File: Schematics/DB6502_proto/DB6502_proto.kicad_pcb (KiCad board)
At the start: 2 copper layers, 143.5 x 138.4 mm, 96 parts, among them J1 Power plug, J10 System Bus, J11 LCD Port, J12 VIA Ports, J13 UART GPIO, J2 Controls, J3 AVR ISP, J4 Debug USB, J5 JPR, J6 Debug UART, J7 UART A, J8 UART B, J9 I/O Bus, SW1 Reset, U1 71256, U10 FT230XS, U11 74HC595, U12 74HC157, U13 ATmega644PA-PU, U14 74AC74, U15 DS1813, U16 74AC74, U17 74AC08, U18 SC26C92, U19 65C22S, U2 71256, U20 74AC04, U21 74AC574, U3 28C256, U4 65C02S, U5 74AC74, U6 74AC138, U7 22V10C, U8 74AC04, U9 74HC21, X1 8MHz, Y1 20MHz, Y2 3,6864MHz

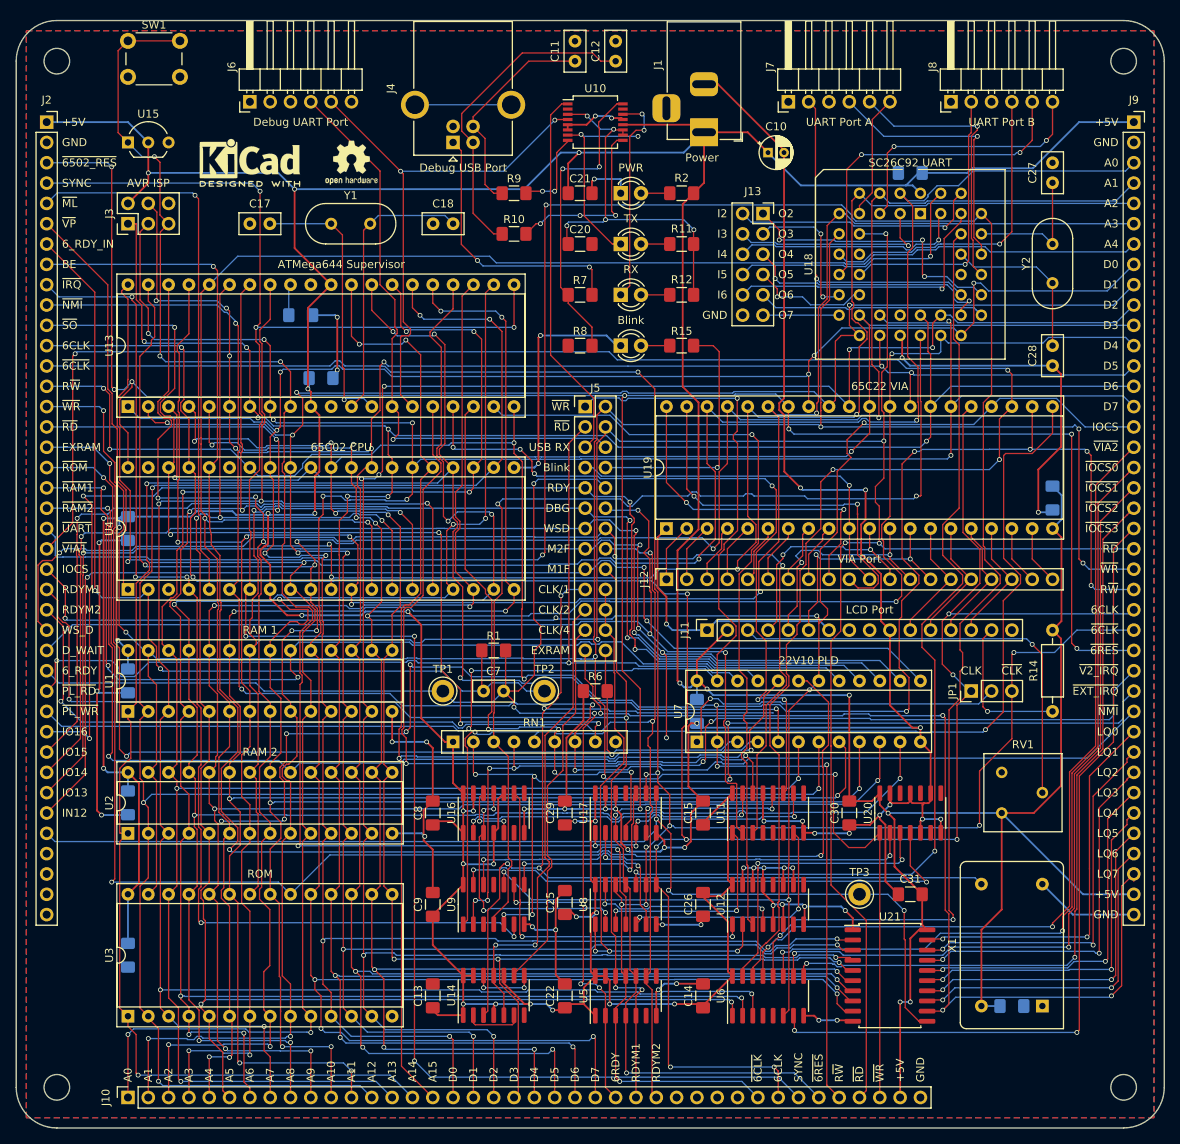
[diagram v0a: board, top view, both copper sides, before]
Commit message: Added bus labels
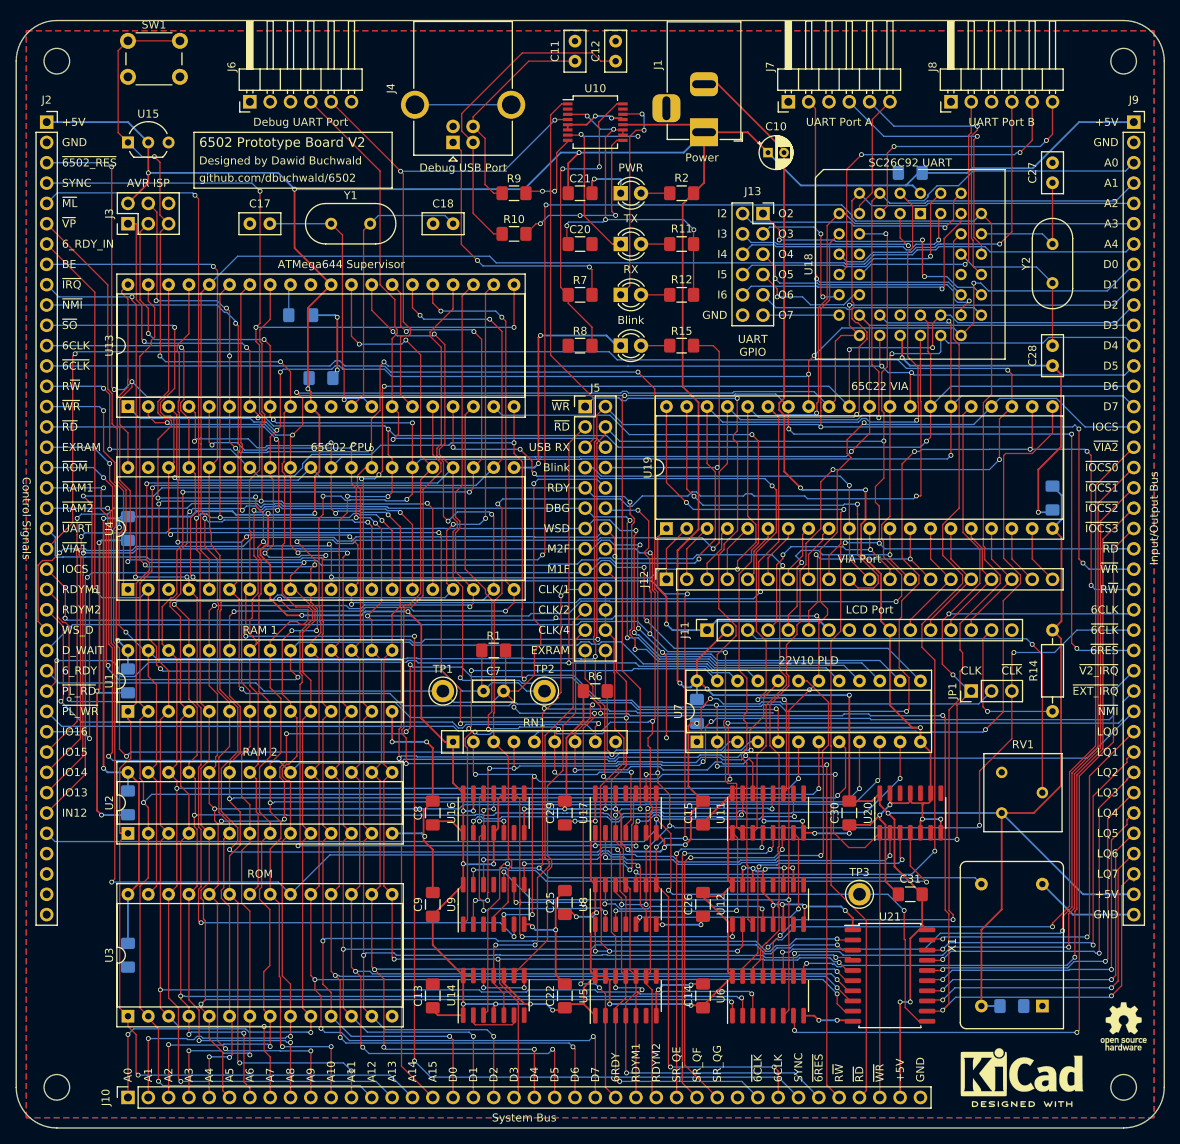
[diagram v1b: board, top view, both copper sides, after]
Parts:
- removed the REF** at (63.5, 53.3)
- removed the REF** at (50.8, 53.3)
- added REF**: OSHW-Logo_5.7x6mm_SilkScreen, Symbol:OSHW-Logo_5.7x6mm_SilkScreen, F.Cu at (160.0, 161.3)
- added REF**: KiCad-Logo2_6mm_SilkScreen, Symbol:KiCad-Logo2_6mm_SilkScreen, F.Cu at (147.3, 167.0)
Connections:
- J10 pad 28: Net-(J10-Pad28) -> SR_QE
- J10 pad 29: Net-(J10-Pad29) -> SR_QF
- J10 pad 30: Net-(J10-Pad30) -> SR_QG
- U11 pad 4: Net-(U11-Pad4) -> SR_QE
- U11 pad 5: Net-(U11-Pad5) -> SR_QF
- U11 pad 6: Net-(U11-Pad6) -> SR_QG
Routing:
- net SR_QG: track 0.00 -> 46.1 mm, vias 0 -> 2
- net SR_QF: track 0.00 -> 44.5 mm, vias 0 -> 2
- net SR_QE: track 0.00 -> 43.4 mm, vias 0 -> 2
- net ROM_~CS: track 175.4 -> 176.0 mm
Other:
- board text added: "6502 Prototype Board V2"
- board text added: "Control Signals"
- board text added: "Designed by Dawid Buchwald"
- board text added: "Input/Output Bus"
- board text added: "SR_QE"
- board text added: "SR_QF"
- board text added: "SR_QG"
- board text added: "System Bus"
- board text added: "UART GPIO"
- board text added: "github.com/dbuchwald/6502"

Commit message: Some minor changes to PCB
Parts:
- moved J3 7.73 mm to (43.2, 59.7), turned to 270 degrees
- moved SW1 1.27 mm to (35.6, 39.4)
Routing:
- net +5V: track 839.9 -> 847.7 mm
- net d6: track 353.7 -> 349.7 mm
- net d5: track 344.5 -> 340.8 mm
- net d7: track 378.2 -> 381.9 mm, vias 12 -> 13
- net ~RES: track 201.3 -> 198.8 mm, vias 8 -> 7
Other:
- board text added: "RST"

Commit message: Added one last line to the system
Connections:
- J10 pad 31: Net-(J10-Pad31) -> BE
- J2 pad 37: Net-(J2-Pad37) -> EXT_BE
- J2 pad 38: Net-(J2-Pad38) -> CLK_1
- J2 pad 39: Net-(J2-Pad39) -> CLK_2
- J2 pad 40: Net-(J2-Pad40) -> CLK_4
- RN1 pad 9: Net-(RN1-Pad9) -> EXT_BE
- U17 pad 11: Net-(U17-Pad11) -> BE
- U17 pad 12: GND -> Net-(U17-Pad12)
- U17 pad 13: GND -> EXT_BE
- U8 pad 4: BE -> Net-(U17-Pad12)
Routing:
- net EXT_BE: track 0.00 -> 92.2 mm, vias 0 -> 3
- net CLK_4: track 47.3 -> 109.7 mm, vias 0 -> 1
- net CLK_1: track 148.3 -> 208.8 mm, vias 4 -> 5
- net CLK_2: track 59.2 -> 118.9 mm
- net BE: track 156.9 -> 208.7 mm, vias 3 -> 6
- net Net-(U17-Pad12): track 0.00 -> 23.9 mm, vias 0 -> 4
- net GND: track 558.4 -> 553.3 mm, vias 52 -> 51
- net ~WR: track 363.7 -> 365.0 mm
- net RDY_M1F: track 157.3 -> 158.1 mm
- net LATCH_CP: track 137.7 -> 137.0 mm
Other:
- board text added: "EXT_BE"
- board text added: "L_CP"

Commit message: PCB RC1
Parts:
- added QR*****: https://tinyurl.com/ghdb6502, DB6502_proto:ghdb6502_03, F.Cu at (27.9, 159.4)
- added TP4: TestPoint, TestPoint:TestPoint_Keystone_5005-5009_Compact, F.Cu at (113.7, 78.7)
- REF** (x4): value MountingHole_3.2mm_M3 -> MountingHole_3.2mm_M3_Pad; footprint MountingHole:MountingHole_3.2mm_M3 -> MountingHole:MountingHole_3.2mm_M3_Pad
- moved C7 2.54 mm to (82.5, 119.4), turned to 180 degrees
- moved C10 1.42 mm to (116.2, 53.3)
- turned R1 to 180 degrees
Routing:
- net R~W: track 361.2 -> 303.5 mm, vias 17 -> 12
- net GND: track 553.3 -> 510.8 mm
- net +5V: track 847.7 -> 849.1 mm
- net d5: track 340.8 -> 342.1 mm
- net 6502_RDY: track 179.1 -> 177.9 mm, vias 7 -> 8
- net UART_B_TxD: track 43.0 -> 44.2 mm
- net ~VIA1: track 246.1 -> 247.1 mm
- net ~6502_RES: track 322.6 -> 323.4 mm
- net a0: track 313.9 -> 313.2 mm
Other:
- board text added: "LCD Contrast"
- board text added: "PLD Clock"
- board text added: "RESET"
- board text added: "SC26C92 Dual UART"
- board text removed: "SC26C92 UART"

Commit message: PCB RC2
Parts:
- C10: footprint Capacitor_THT:CP_Radial_D4.0mm_P2.00mm -> Capacitor_THT:CP_Radial_D4.0mm_P1.50mm
- C11, C12, C17, C18, C27, C28, C7: footprint Capacitor_THT:C_Disc_D5.0mm_W2.5mm_P2.50mm -> Capacitor_SMD:C_1206_3216Metric_Pad1.33x1.80mm_HandSolder
- moved C17 2.25 mm to (53.0, 61.0)
- moved C28 1.87 mm to (151.1, 76.8)
- moved C27 1.48 mm to (151.1, 54.4)
- moved C7 1.27 mm to (81.3, 119.4)
- turned C18 to 180 degrees
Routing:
- net Net-(C18-Pad2): track 35.0 -> 30.1 mm, vias 0 -> 1
- net 6502_RDY: track 177.9 -> 179.5 mm, vias 8 -> 9
- net Net-(C17-Pad2): track 34.3 -> 33.0 mm, vias 1 -> 2
- net 6502_RDY_IN: track 118.5 -> 119.4 mm, vias 2 -> 3
- net SYNC: track 245.9 -> 246.5 mm
- net Net-(C12-Pad1): track 40.6 -> 39.9 mm
- net GND: track 510.8 -> 511.3 mm, vias 51 -> 52
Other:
- rule pad_to_mask_clearance: 0.051 -> 0

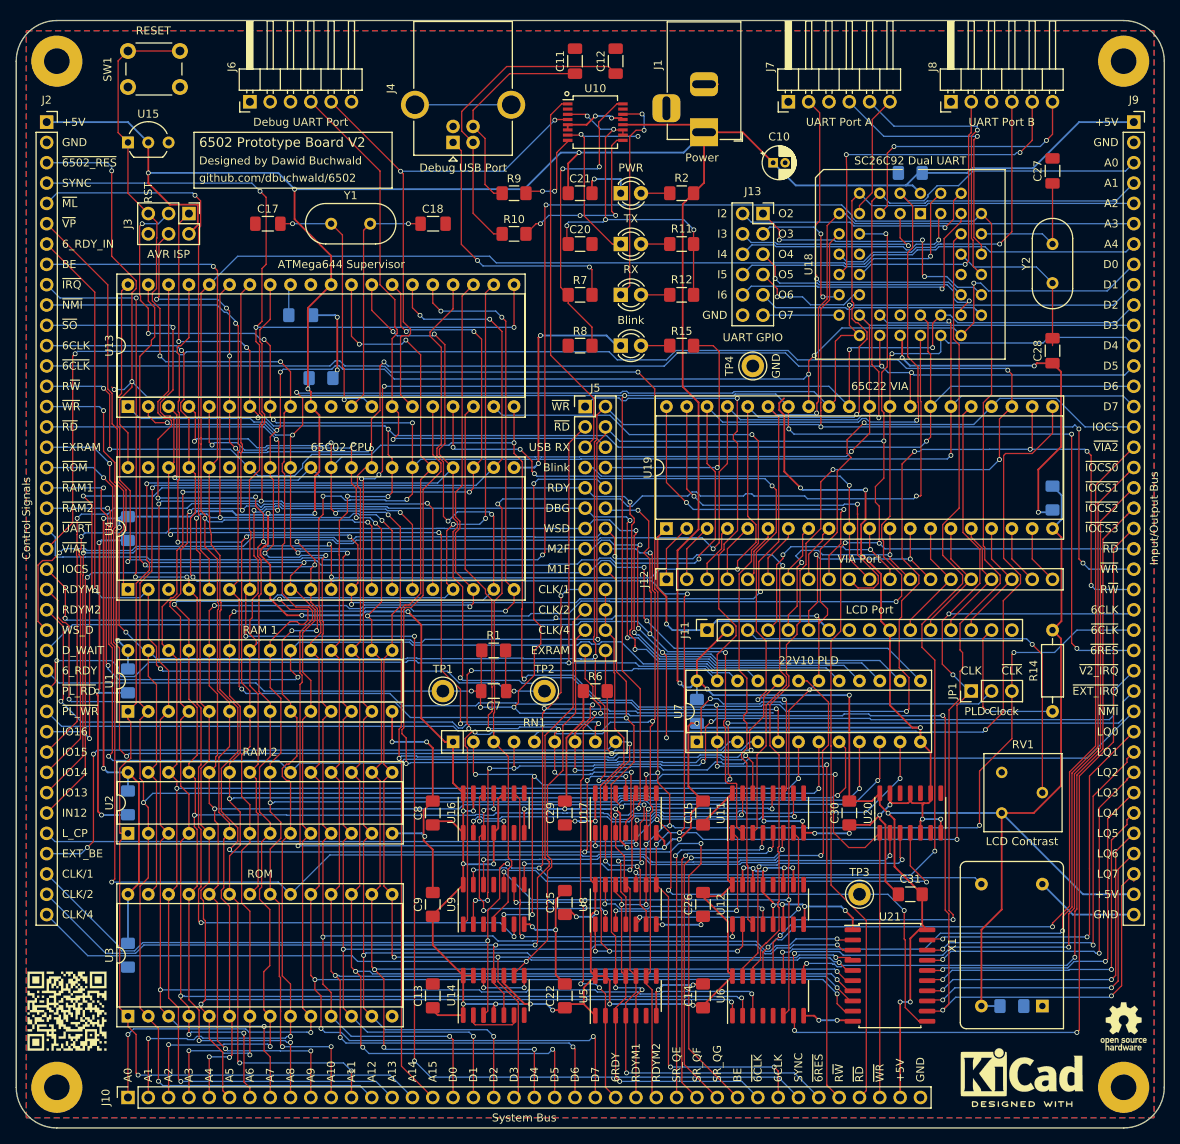
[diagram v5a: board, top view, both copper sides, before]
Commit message: Last minute updates (remove VCC from AVRISP)
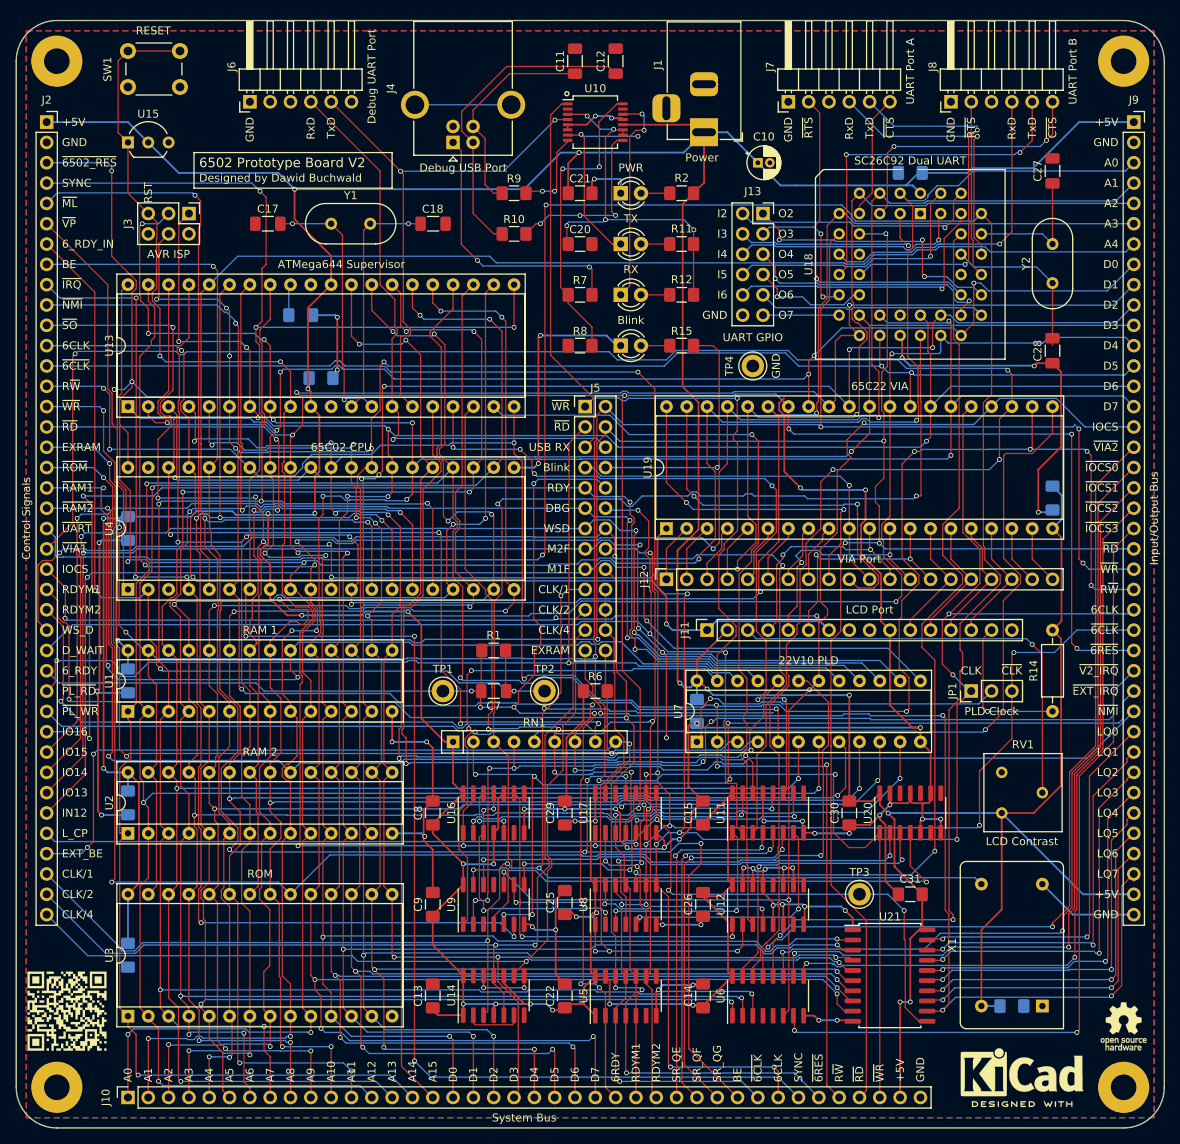
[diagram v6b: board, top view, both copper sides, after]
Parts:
- moved C10 1.91 mm to (114.3, 53.3)
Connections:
- J3 pad 2: +5V -> Net-(J3-Pad2)
- U16 pad 1: +5V -> ~RES
- U16 pad 13: +5V -> ~RES
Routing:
- net +5V: track 849.1 -> 829.4 mm, vias 32 -> 29
- net ~RES: track 198.8 -> 206.0 mm, vias 7 -> 8
- net ~VIA1_IRQ: track 138.6 -> 139.5 mm
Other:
- board text added: "RxD"
- board text added: "TxD"
- board text added: "~CTS"
- board text added: "~RTS"
- board text removed: "github.com/dbuchwald/6502"

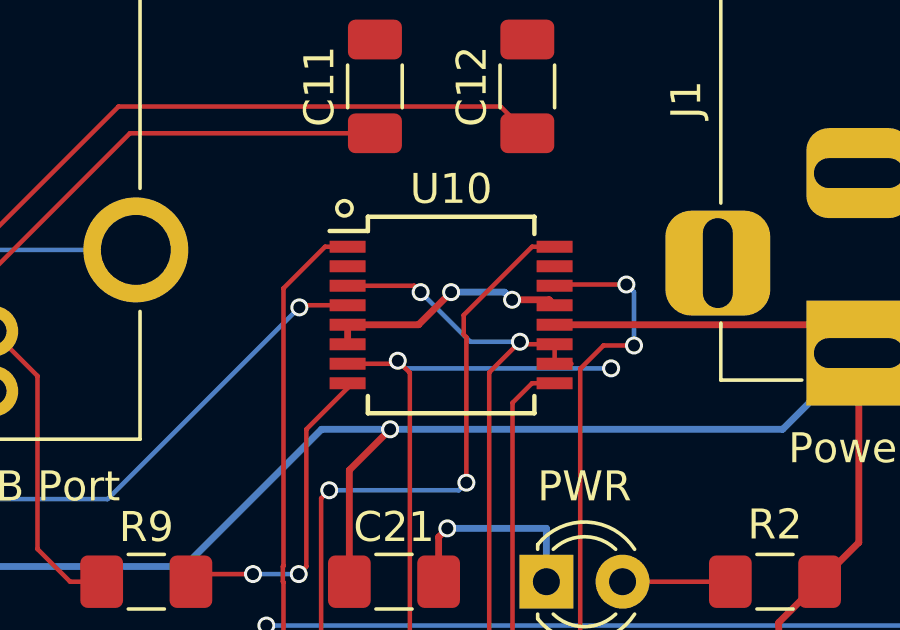
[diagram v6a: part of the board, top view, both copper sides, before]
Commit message: Working on massively redesigned board
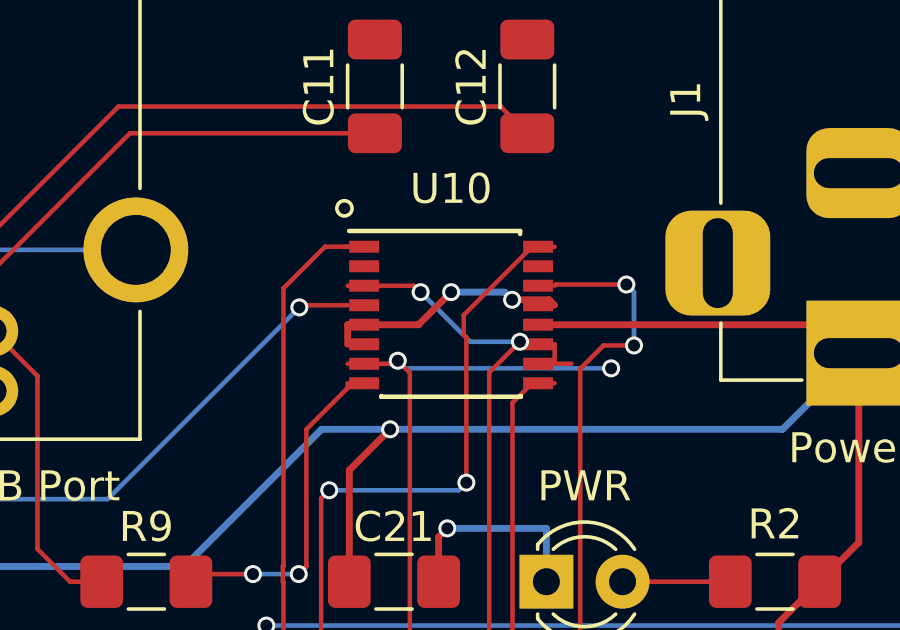
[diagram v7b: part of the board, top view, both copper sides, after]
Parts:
- U10: footprint Package_SO:SSOP-16_5.3x6.2mm_P0.65mm -> Package_SO:SSOP-16_4.4x5.2mm_P0.65mm
